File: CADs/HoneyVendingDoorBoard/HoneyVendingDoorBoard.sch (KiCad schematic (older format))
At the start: 34 parts, among them J1 Conn_01x08_Female, J2 Door5, J3 Door6, J4 Door1, J5 Door2, J6 Door3, J7 Door4, Q1 IRLZ34N, Q2 IRLZ34N, Q3 IRLZ34N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

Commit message: Reworded PCBs and added PCB pdfs
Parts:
- J1: footprint Connector_Molex:Molex_Mini-Fit_Jr_5566-08A_2x04_P4.20mm_Vertical -> Connector_PinHeader_2.54mm:PinHeader_2x04_P2.54mm_Vertical
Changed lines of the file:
@@
 F 0 "J1" H 1744 3525 50  0000 C CNN
 F 1 "Conn_01x08_Female" H 1744 3616 50  0000 C CNN
-F 2 "Connector_Molex:Molex_Mini-Fit_Jr_5566-08A_2x04_P4.20mm_Vertical" H 1850 4150 50  0001 C CNN
+F 2 "Connector_PinHeader_2.54mm:PinHeader_2x04_P2.54mm_Vertical" H 1850 4150 50  0001 C CNN
 F 3 "~" H 1850 4150 50  0001 C CNN
 	1    1850 4150

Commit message: Updates boards
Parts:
- J2, J3, J4, J5, J6, J7: footprint Connector_JST:JST_XH_B02B-XH-AM_1x02_P2.50mm_Vertical -> Connector_PinHeader_2.54mm:PinHeader_1x02_P2.54mm_Vertical
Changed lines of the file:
@@
 F 0 "J4" H 6222 1480 50  0000 R CNN
 F 1 "Door1" H 6222 1571 50  0000 R CNN
-F 2 "Connector_JST:JST_XH_B02B-XH-AM_1x02_P2.50mm_Vertical" H 6250 1600 50  0001 C CNN
+F 2 "Connector_PinHeader_2.54mm:PinHeader_1x02_P2.54mm_Vertical" H 6250 1600 50  0001 C CNN
 F 3 "~" H 6250 1600 50  0001 C CNN
 	1    6250 1600
@@
 F 0 "J5" H 6222 2430 50  0000 R CNN
 F 1 "Door2" H 6222 2521 50  0000 R CNN
-F 2 "Connector_JST:JST_XH_B02B-XH-AM_1x02_P2.50mm_Vertical" H 6250 2550 50  0001 C CNN
+F 2 "Connector_PinHeader_2.54mm:PinHeader_1x02_P2.54mm_Vertical" H 6250 2550 50  0001 C CNN
 F 3 "~" H 6250 2550 50  0001 C CNN
 	1    6250 2550
@@
 F 0 "J6" H 6222 3480 50  0000 R CNN
 F 1 "Door3" H 6222 3571 50  0000 R CNN
-F 2 "Connector_JST:JST_XH_B02B-XH-AM_1x02_P2.50mm_Vertical" H 6250 3600 50  0001 C CNN
+F 2 "Connector_PinHeader_2.54mm:PinHeader_1x02_P2.54mm_Vertical" H 6250 3600 50  0001 C CNN
 F 3 "~" H 6250 3600 50  0001 C CNN
 	1    6250 3600
@@
 F 0 "J7" H 6222 4480 50  0000 R CNN
 F 1 "Door4" H 6222 4571 50  0000 R CNN
-F 2 "Connector_JST:JST_XH_B02B-XH-AM_1x02_P2.50mm_Vertical" H 6250 4600 50  0001 C CNN
+F 2 "Connector_PinHeader_2.54mm:PinHeader_1x02_P2.54mm_Vertical" H 6250 4600 50  0001 C CNN
 F 3 "~" H 6250 4600 50  0001 C CNN
 	1    6250 4600
@@
 F 0 "J2" H 6172 5430 50  0000 R CNN
 F 1 "Door5" H 6172 5521 50  0000 R CNN
-F 2 "Connector_JST:JST_XH_B02B-XH-AM_1x02_P2.50mm_Vertical" H 6200 5550 50  0001 C CNN
+F 2 "Connector_PinHeader_2.54mm:PinHeader_1x02_P2.54mm_Vertical" H 6200 5550 50  0001 C CNN
 F 3 "~" H 6200 5550 50  0001 C CNN
 	1    6200 5550
@@
 F 0 "J3" H 6172 6430 50  0000 R CNN
 F 1 "Door6" H 6172 6521 50  0000 R CNN
-F 2 "Connector_JST:JST_XH_B02B-XH-AM_1x02_P2.50mm_Vertical" H 6200 6550 50  0001 C CNN
+F 2 "Connector_PinHeader_2.54mm:PinHeader_1x02_P2.54mm_Vertical" H 6200 6550 50  0001 C CNN
 F 3 "~" H 6200 6550 50  0001 C CNN
 	1    6200 6550

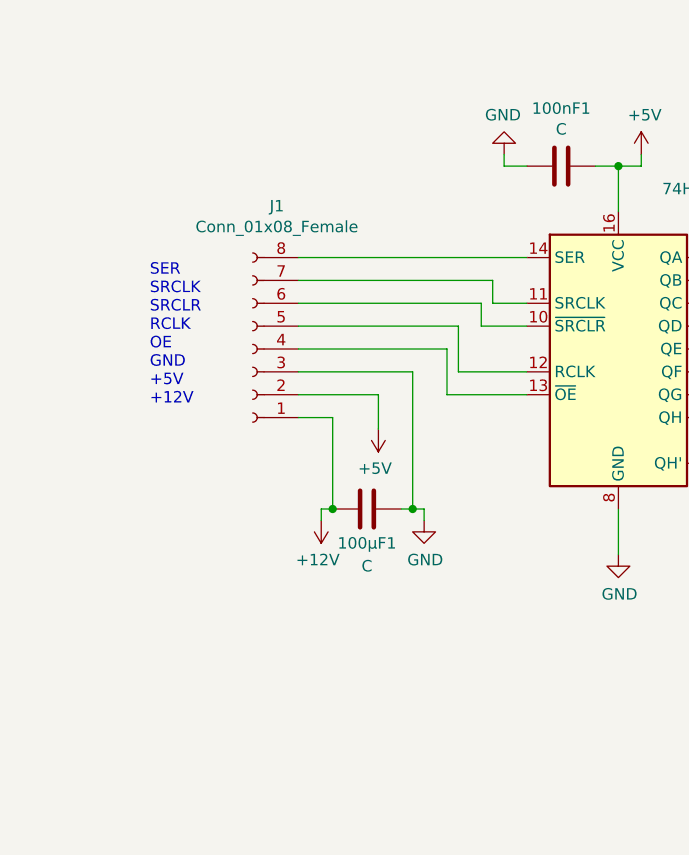
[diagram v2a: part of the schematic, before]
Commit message: Applying nicos feedback for boards
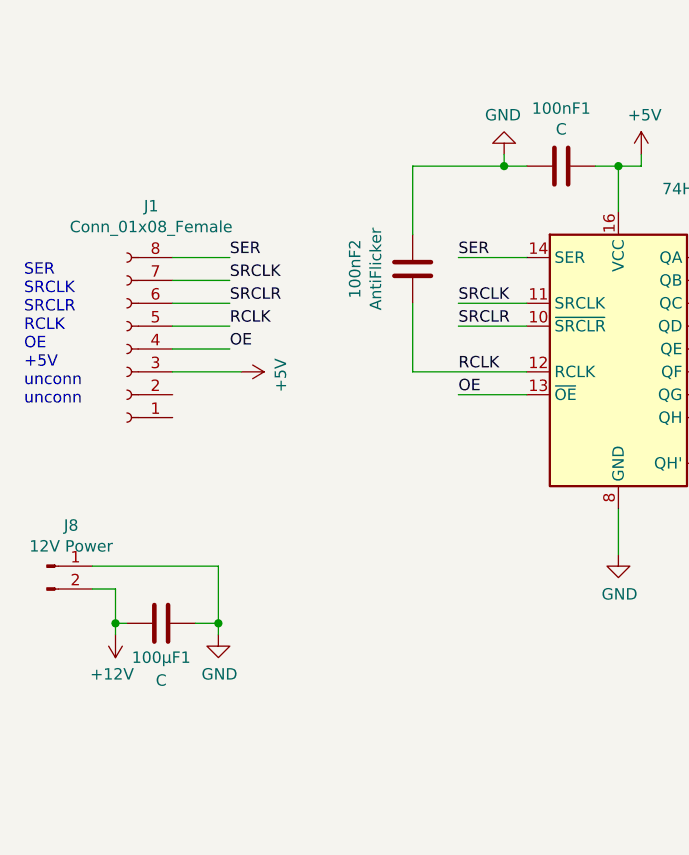
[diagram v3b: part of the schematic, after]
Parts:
- added 100nF2: AntiFlicker, Capacitor_THT:C_Disc_D6.0mm_W2.5mm_P5.00mm, symbol Device:C
- added J8: 12V Power, Connector_PinHeader_2.54mm:PinHeader_1x02_P2.54mm_Vertical, symbol Connector:Conn_01x02_Male
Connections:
- net +12V: now also J8.2 (Pin_2); no longer J1.1 (Pin_1)
- net +5V: now also J1.3 (Pin_3); no longer J1.2 (Pin_2)
- net GND: now also 100nF2.1, J8.1 (Pin_1); no longer J1.3 (Pin_3)
- net SRCLR: now reaches J1.6 (Pin_6), U1.10 (~SRCLR)
- net SRCLK: now reaches J1.7 (Pin_7), U1.11 (SRCLK)
- net RCLK: now reaches J1.5 (Pin_5), U1.12 (RCLK)
- net RCLK: now also 100nF2.2
- net OE: now reaches J1.4 (Pin_4), U1.13 (~OE)
- net SER: now reaches J1.8 (Pin_8), U1.14 (SER)
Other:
- note added: "SER\nSRCLK\nSRCLR\nRCLK\nOE\n+5V\nunconn\nunconn"
- note removed: "SER\nSRCLK\nSRCLR\nRCLK\nOE\nGND\n+5V\n+12V"
- moved on the sheet: 100µF1, J1
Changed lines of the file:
@@
 L Connector:Conn_01x08_Female J1
 U 1 1 5E8B4A43
-P 1850 4150
-F 0 "J1" H 1744 3525 50  0000 C CNN
-F 1 "Conn_01x08_Female" H 1744 3616 50  0000 C CNN
-F 2 "Connector_PinHeader_2.54mm:PinHeader_2x04_P2.54mm_Vertical" H 1850 4150 50  0001 C CNN
-F 3 "~" H 1850 4150 50  0001 C CNN
-	1    1850 4150
+P 1300 4150
+F 0 "J1" H 1194 3525 50  0000 C CNN
+F 1 "Conn_01x08_Female" H 1194 3616 50  0000 C CNN
+F 2 "Connector_PinHeader_2.54mm:PinHeader_2x04_P2.54mm_Vertical" H 1300 4150 50  0001 C CNN
+F 3 "~" H 1300 4150 50  0001 C CNN
+	1    1300 4150
 	-1   0    0    1
 $EndComp
-Text Notes 1400 4400 0    50   ~ 0
-SER\nSRCLK\nSRCLR\nRCLK\nOE\nGND\n+5V\n+12V
-Wire Wire Line
-	3050 3750 2050 3750
-Wire Wire Line
-	3050 3950 2900 3950
-Wire Wire Line
-	2900 3950 2900 3850
-Wire Wire Line
-	2900 3850 2050 3850
-Wire Wire Line
-	2050 3950 2850 3950
-Wire Wire Line
-	2850 3950 2850 4050
-Wire Wire Line
-	2850 4050 3050 4050
-Wire Wire Line
-	3050 4250 2750 4250
-Wire Wire Line
-	2750 4250 2750 4050
-Wire Wire Line
-	2750 4050 2050 4050
-Wire Wire Line
-	2700 4150 2700 4350
-Wire Wire Line
-	2700 4350 3050 4350
-Wire Wire Line
-	2050 4150 2700 4150
+Text Notes 850  4400 0    50   ~ 0
+SER\nSRCLK\nSRCLR\nRCLK\nOE\n+5V\nunconn\nunconn
 $Comp
 L power:GND #PWR0116
 U 1 1 5E8CC3A4
-P 2600 4900
-F 0 "#PWR0116" H 2600 4650 50  0001 C CNN
-F 1 "GND" H 2605 4727 50  0000 C CNN
-F 2 "" H 2600 4900 50  0001 C CNN
-F 3 "" H 2600 4900 50  0001 C CNN
-	1    2600 4900
+P 1700 5400
+F 0 "#PWR0116" H 1700 5150 50  0001 C CNN
+F 1 "GND" H 1705 5227 50  0000 C CNN
+F 2 "" H 1700 5400 50  0001 C CNN
+F 3 "" H 1700 5400 50  0001 C CNN
+	1    1700 5400
 	1    0    0    -1
 $EndComp
@@
 L power:+5V #PWR0117
 U 1 1 5E8CC416
-P 2400 4500
-F 0 "#PWR0117" H 2400 4350 50  0001 C CNN
-F 1 "+5V" H 2415 4673 50  0000 C CNN
-F 2 "" H 2400 4500 50  0001 C CNN
-F 3 "" H 2400 4500 50  0001 C CNN
-	1    2400 4500
-	-1   0    0    1
+P 1800 4250
+F 0 "#PWR0117" H 1800 4100 50  0001 C CNN
+F 1 "+5V" H 1815 4423 50  0000 C CNN
+F 2 "" H 1800 4250 50  0001 C CNN
+F 3 "" H 1800 4250 50  0001 C CNN
+	1    1800 4250
+	0    1    1    0
 $EndComp
 $Comp
 L power:+12V #PWR0118
 U 1 1 5E8CC4D1
-P 2150 4900
-F 0 "#PWR0118" H 2150 4750 50  0001 C CNN
-F 1 "+12V" H 2165 5073 50  0000 C CNN
-F 2 "" H 2150 4900 50  0001 C CNN
-F 3 "" H 2150 4900 50  0001 C CNN
-	1    2150 4900
+P 1250 5400
+F 0 "#PWR0118" H 1250 5250 50  0001 C CNN
+F 1 "+12V" H 1265 5573 50  0000 C CNN
+F 2 "" H 1250 5400 50  0001 C CNN
+F 3 "" H 1250 5400 50  0001 C CNN
+	1    1250 5400
 	-1   0    0    1
 $EndComp
-Wire Wire Line
-	2050 4250 2550 4250
-Wire Wire Line
-	2050 4350 2400 4350
-Wire Wire Line
-	2400 4350 2400 4500
-Wire Wire Line
-	2050 4450 2200 4450
 $Comp
 L Device:C 100µF1
 U 1 1 5E8DD695
-P 2350 4850
-F 0 "100µF1" V 2200 4850 50  0000 C CNN
-F 1 "C" V 2100 4850 50  0000 C CNN
-F 2 "Capacitor_THT:CP_Radial_D8.0mm_P3.50mm" H 2388 4700 50  0001 C CNN
-F 3 "~" H 2350 4850 50  0001 C CNN
-	1    2350 4850
+P 1450 5350
+F 0 "100µF1" V 1300 5350 50  0000 C CNN
+F 1 "C" V 1200 5350 50  0000 C CNN
+F 2 "Capacitor_THT:CP_Radial_D8.0mm_P3.50mm" H 1488 5200 50  0001 C CNN
+F 3 "~" H 1450 5350 50  0001 C CNN
+	1    1450 5350
 	0    -1   -1   0
 $EndComp
 Wire Wire Line
-	2150 4900 2150 4850
+	1250 5400 1250 5350
 Wire Wire Line
-	2150 4850 2200 4850
+	1250 5350 1300 5350
 Wire Wire Line
-	2200 4450 2200 4850
-Connection ~ 2200 4850
-Wire Wire Line
-	2600 4900 2600 4850
-Wire Wire Line
-	2600 4850 2550 4850
-Wire Wire Line
-	2550 4250 2550 4850
-Connection ~ 2550 4850
-Wire Wire Line
-	2550 4850 2500 4850
+	1700 5400 1700 5350
 Text Notes 4200 4850 0    50   ~ 0
 QG, QH and QH'\nare outputs. No\nneed to pull down
+Wire Wire Line
+	1600 5350 1700 5350
+Wire Wire Line
+	1500 4250 1800 4250
+Wire Wire Line
+	1500 3750 1750 3750
+Wire Wire Line
+	1500 3850 1750 3850
+Wire Wire Line
+	1500 3950 1750 3950
+Wire Wire Line
+	1500 4050 1750 4050
+Wire Wire Line
+	1500 4150 1750 4150
+Text Label 1750 3750 0    50   ~ 0
+SER
+Text Label 1750 3850 0    50   ~ 0
+SRCLK
+Text Label 1750 3950 0    50   ~ 0
+SRCLR
+Text Label 1750 4050 0    50   ~ 0
+RCLK
+Text Label 1750 4150 0    50   ~ 0
+OE
+Wire Wire Line
+	3050 3750 2750 3750
+Wire Wire Line
+	2750 3950 3050 3950
+Wire Wire Line
+	2750 4050 3050 4050
+Wire Wire Line
+	3050 4350 2750 4350
+Text Label 2750 3750 0    50   ~ 0
+SER
+Text Label 2750 3950 0    50   ~ 0
+SRCLK
+Text Label 2750 4050 0    50   ~ 0
+SRCLR
+Text Label 2750 4250 0    50   ~ 0
+RCLK
+Text Label 2750 4350 0    50   ~ 0
+OE
+$Comp
+L Device:C 100nF2
+U 1 1 5E9546D2
+P 2550 3800
+F 0 "100nF2" V 2298 3800 50  0000 C CNN
+F 1 "AntiFlicker" V 2389 3800 50  0000 C CNN
+F 2 "Capacitor_THT:C_Disc_D6.0mm_W2.5mm_P5.00mm" H 2588 3650 50  0001 C CNN
+F 3 "~" H 2550 3800 50  0001 C CNN
+	1    2550 3800
+	1    0    0    -1
+$EndComp
+Wire Wire Line
+	2550 4250 2550 3950
+Wire Wire Line
+	2550 4250 3050 4250
+Wire Wire Line
+	2550 3650 2550 3350
+Wire Wire Line
+	2550 3350 2950 3350
+Connection ~ 2950 3350
+$Comp
+L Connector:Conn_01x02_Male J8
+U 1 1 5E9601AF
+P 950 5100
+F 0 "J8" H 1056 5278 50  0000 C CNN
+F 1 "12V Power" H 1056 5187 50  0000 C CNN
+F 2 "Connector_PinHeader_2.54mm:PinHeader_1x02_P2.54mm_Vertical" H 950 5100 50  0001 C CNN
+F 3 "~" H 950 5100 50  0001 C CNN
+	1    950  5100
+	1    0    0    -1
+$EndComp
+Wire Wire Line
+	1150 5200 1250 5200
+Wire Wire Line
+	1250 5200 1250 5350
+Connection ~ 1250 5350
+Wire Wire Line
+	1150 5100 1700 5100
+Wire Wire Line
+	1700 5100 1700 5350
+Connection ~ 1700 5350
 $EndSCHEMATC

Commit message: Split Main Board into Main Board and Button Board
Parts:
- removed J8: 12V Power, Connector_PinHeader_2.54mm:PinHeader_1x02_P2.54mm_Vertical, symbol Connector:Conn_01x02_Male
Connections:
- net +12V: now also J1.2 (Pin_2)
- net +5V: now also J1.4 (Pin_4); no longer J1.3 (Pin_3)
- net GND: now also J1.1 (Pin_1)
- net OE: now also J1.3 (Pin_3); no longer J1.4 (Pin_4)
- net RCLK: now also J1.6 (Pin_6); no longer J1.5 (Pin_5)
- net SER: now also J1.7 (Pin_7); no longer J1.8 (Pin_8)
- net SRCLK: now also J1.8 (Pin_8); no longer J1.7 (Pin_7)
- net SRCLR: now also J1.5 (Pin_5); no longer J1.6 (Pin_6)
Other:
- note added: "SRCLK\nSER\nRCLK\nSRCLR\n5V\nOE\n12V\nGND"
- note removed: "SER\nSRCLK\nSRCLR\nRCLK\nOE\n+5V\nunconn\nunconn"
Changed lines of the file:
@@
 $EndComp
 Text Notes 850  4400 0    50   ~ 0
-SER\nSRCLK\nSRCLR\nRCLK\nOE\n+5V\nunconn\nunconn
+SRCLK\nSER\nRCLK\nSRCLR\n5V\nOE\n12V\nGND
 $Comp
 L power:GND #PWR0116
@@
 L power:+5V #PWR0117
 U 1 1 5E8CC416
-P 1800 4250
-F 0 "#PWR0117" H 1800 4100 50  0001 C CNN
-F 1 "+5V" H 1815 4423 50  0000 C CNN
-F 2 "" H 1800 4250 50  0001 C CNN
-F 3 "" H 1800 4250 50  0001 C CNN
-	1    1800 4250
+P 1850 4150
+F 0 "#PWR0117" H 1850 4000 50  0001 C CNN
+F 1 "+5V" H 1865 4323 50  0000 C CNN
+F 2 "" H 1850 4150 50  0001 C CNN
+F 3 "" H 1850 4150 50  0001 C CNN
+	1    1850 4150
 	0    1    1    0
 $EndComp
@@
 	1600 5350 1700 5350
 Wire Wire Line
-	1500 4250 1800 4250
-Wire Wire Line
 	1500 3750 1750 3750
 Wire Wire Line
@@
 Wire Wire Line
 	1500 4050 1750 4050
-Wire Wire Line
-	1500 4150 1750 4150
+Text Label 1750 3850 0    50   ~ 0
+SER
 Text Label 1750 3750 0    50   ~ 0
-SER
-Text Label 1750 3850 0    50   ~ 0
 SRCLK
+Text Label 1750 4050 0    50   ~ 0
+SRCLR
 Text Label 1750 3950 0    50   ~ 0
-SRCLR
-Text Label 1750 4050 0    50   ~ 0
 RCLK
-Text Label 1750 4150 0    50   ~ 0
+Text Label 1750 4250 0    50   ~ 0
 OE
 Wire Wire Line
@@
 Connection ~ 2950 3350
 $Comp
-L Connector:Conn_01x02_Male J8
-U 1 1 5E9601AF
-P 950 5100
-F 0 "J8" H 1056 5278 50  0000 C CNN
-F 1 "12V Power" H 1056 5187 50  0000 C CNN
-F 2 "Connector_PinHeader_2.54mm:PinHeader_1x02_P2.54mm_Vertical" H 950 5100 50  0001 C CNN
-F 3 "~" H 950 5100 50  0001 C CNN
-	1    950  5100
+L power:+12V #PWR?
+U 1 1 5E9572B2
+P 1950 4300
+F 0 "#PWR?" H 1950 4150 50  0001 C CNN
+F 1 "+12V" H 1965 4473 50  0000 C CNN
+F 2 "" H 1950 4300 50  0001 C CNN
+F 3 "" H 1950 4300 50  0001 C CNN
+	1    1950 4300
+	0    1    1    0
+$EndComp
+$Comp
+L power:GND #PWR?
+U 1 1 5E9574CA
+P 1800 4500
+F 0 "#PWR?" H 1800 4250 50  0001 C CNN
+F 1 "GND" H 1805 4327 50  0000 C CNN
+F 2 "" H 1800 4500 50  0001 C CNN
+F 3 "" H 1800 4500 50  0001 C CNN
+	1    1800 4500
 	1    0    0    -1
 $EndComp
 Wire Wire Line
-	1150 5200 1250 5200
+	1500 4350 1950 4350
 Wire Wire Line
-	1250 5200 1250 5350
-Connection ~ 1250 5350
+	1950 4350 1950 4300
 Wire Wire Line
-	1150 5100 1700 5100
+	1800 4500 1800 4450
 Wire Wire Line
-	1700 5100 1700 5350
-Connection ~ 1700 5350
+	1800 4450 1500 4450
+Wire Wire Line
+	1500 4250 1750 4250
+Wire Wire Line
+	1500 4150 1850 4150
 $EndSCHEMATC
